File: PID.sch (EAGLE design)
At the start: 11 parts, among them IC1 UA741CPE4, IC2 UA741CPE4, IC3 UA741CPE4

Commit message: paf
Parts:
- added CONSIGNE, RETOUR, RETOUR1: (no value), pinhead:PINHD-1X1
- added IC4, IC5: UA741CPE4, SamacSys_Parts:UA741CPE4
- added R1, R3, R4, R6: 22k, rcl:R-EU_0204/7
- added R10, R7, R8, R9: 10k, rcl:R-EU_0204/7
- added R11: 2.5k, rcl:R-EU_0204/7
- added R5: (no value), rcl:R-EU_0204/7
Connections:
- new net CONSIGNE: CONSIGNE.1, R4.1
- new net N$13: IC5.IN+, R4.2, R6.2
- new net N$15: IC4.IN-, R10.1, R7.2, R8.2, R9.2
- new net N$17: C3.+, R5.2
- new net N$18: IC4.IN+, R11.2
- new net N$9: IC5.IN-, R1.1, R3.2
- new net OUTPUT: IC4.OUT, R10.2, RETOUR1.1
- new net RETOUR: R3.1, R5.1, RETOUR.1
- net GND: now also R11.1, R6.1
- net N$10: now also R9.1
- net N$2: now also R7.1
- net N$4: now also R8.1
- net N$7: now also IC5.OUT, R1.2, R2.1
- net V+: now also IC4.VCC+, IC5.VCC+
- net V-: now also IC4.VCC-, IC5.VCC-
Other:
- moved on the sheet: C1, C2, C3, C4, IC1, IC2, IC3, R2, VR1, VR2, VR3

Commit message: paf
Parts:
- removed C3, C4: (no value), rcl:CPOL-EUE2.5-6
- removed R5: (no value), rcl:R-EU_0204/7
- removed VR1, VR3: T7YA103MT20, PFE:T7YA103MT20
- added CD1, CD2: (no value), rcl:CPOL-EUE2.5-6
- added R13, R14: 22k, rcl:R-EU_0204/7
- added RD: T7YA103MT20, PFE:T7YA103MT20
- R1, R3: value 22k -> (none)
- R11: value 2.5k -> 5k
- R2: value (none) -> T7YA103MT20; device rcl:R-EU_0204/7 -> PFE:T7YA103MT20
- renumbered C1 to CI1, C2 to CI2, VR2 to RI
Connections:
- new net N$16: IC4.IN-, R10.1, R7.2, R8.2
- net N$10: now also RD.C; no longer VR3.C
- net N$12: now also CD2.+, RD.A, RD.B; no longer C4.+, VR3.A, VR3.B
- net N$14: now also CD1.-, CD2.-; no longer C3.-, C4.-
- net N$15: now also IC5.OUT, R13.2; no longer IC4.IN-, R10.1, R7.2, R8.2, R9.2
- net N$17: now also CD1.+, R3.2; no longer C3.+, R5.2
- net N$18: now also R9.2
- net N$2: now also R2.C; no longer VR1.C
- net N$3: now also R1.2, R2.A, R2.B; no longer R2.2, VR1.A, VR1.B
- net N$7: now also R1.1; no longer IC5.OUT, R1.2, R2.1
- net N$9: now also R13.1, R14.2; no longer R1.1, R3.2
- net RETOUR: now also R14.1; no longer R5.1
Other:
- moved on the sheet: IC1, IC3, R1, R3

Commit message: paf
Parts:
- removed RETOUR1: (no value), pinhead:PINHD-1X1
- added OUTPUT: (no value), pinhead:PINHD-1X1
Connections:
- removed net N$7 (its old number): R1.1, RI.A, RI.B
- net N$15: now also R1.1, RI.A, RI.B
- net OUTPUT: now also OUTPUT.1; no longer RETOUR1.1
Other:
- note added: "Comparateur"
- note added: "Sommeur"
- moved on the sheet: CONSIGNE, IC4, IC5, R10, R13, R14, R4, R6, R7, R8, R9, RETOUR

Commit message: paf
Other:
- note added: "Erreur"
- note added: "K = 1/(Ri*Ci)"
- note added: "K = R2/R1"
- note added: "K = Rd*Cd"
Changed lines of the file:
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@@
 <wire x1="261.62" y1="73.66" x2="190.5" y2="73.66" width="0.1524" layer="97"/>
 <text x="193.04" y="30.48" size="1.778" layer="97">Sommeur</text>
+<text x="63.5" y="71.12" size="1.778" layer="91">Erreur</text>
+<text x="147.32" y="48.26" size="1.778" layer="97">K = 1/(Ri*Ci)</text>
+<text x="149.86" y="99.06" size="1.778" layer="97">K = R2/R1</text>
+<text x="149.86" y="-5.08" size="1.778" layer="97">K = Rd*Cd</text>
 </plain>
 <instances>

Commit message: paf
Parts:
- added GND, V+, V-: (no value), pinhead:PINHD-1X1
- added S1, S2, S3: TL36PO, switch:TL36PO
- renumbered R1 to RP1, R2 to RP, R3 to RD1
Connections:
- new net N$12: R7.1, S1.P
- new net N$16: R8.1, S2.P
- new net N$19: R9.1, S3.P
- net GND: now also GND.1, S1.O, S2.O, S3.O
- net N$10: now also S3.S; no longer R9.1
- net N$2: now also S1.S; no longer R7.1
- net N$4: now also S2.S; no longer R8.1
- net V+: now also V+.1
- net V-: now also V-.1
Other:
- moved on the sheet: OUTPUT

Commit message: couocu
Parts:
- removed S1, S2, S3: TL36PO, switch:TL36PO
- added JP1, JP2, JP3: (no value), pinhead:PINHD-1X2
- added R1: 100k, rcl:R-EU_0204/7
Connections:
- net N$15 renamed ERREUR
- net GND: no longer S1.O, S2.O, S3.O
- net N$10: now also JP3.1; no longer S3.S
- net N$12: now also JP1.2; no longer S1.P
- net N$16: now also JP2.2; no longer S2.P
- net N$19: now also JP3.2; no longer S3.P
- net N$2: now also JP1.1; no longer S1.S
- net N$4: now also JP2.1, R1.2; no longer S2.S
- net N$5: now also R1.1
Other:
- note removed: "Erreur"
- moved on the sheet: CI1, CI2, CONSIGNE, GND, IC5, OUTPUT, R13, R14, R4, R6, RETOUR, V+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

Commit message: paf
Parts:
- added R2: 1k, rcl:R-EU_0204/7
- CD1, CD2: value (none) -> 10µ
- CI1, CI2: value (none) -> 470µ
- RD, RP: value T7YA103MT20 -> 10k
- RD1: value (none) -> 200
- RI: value T7YA103MT20 -> 100k
- RP1: value (none) -> 1k
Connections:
- new net N$15: R2.2, RI.A, RI.B
- net ERREUR: now also R2.1; no longer RI.A, RI.B
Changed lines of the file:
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@@
 <attribute name="SPICEPREFIX" value="X"/>
 </part>
-<part name="RP1" library="rcl" library_urn="urn:adsk.eagle:library:334" deviceset="R-EU_" device="0204/7" package3d_urn="urn:adsk.eagle:package:23498/2"/>
+<part name="RP1" library="rcl" library_urn="urn:adsk.eagle:library:334" deviceset="R-EU_" device="0204/7" package3d_urn="urn:adsk.eagle:package:23498/2" value="1k"/>
 <part name="SUPPLY1" library="supply2" library_urn="urn:adsk.eagle:library:372" deviceset="GND" device=""/>
 <part name="P-1" library="supply1" library_urn="urn:adsk.eagle:library:371" deviceset="V-" device=""/>
 <part name="P+2" library="supply1" library_urn="urn:adsk.eagle:library:371" deviceset="V+" device=""/>
-<part name="RP" library="PFE" deviceset="T7YA103MT20" device=""/>
+<part name="RP" library="PFE" deviceset="T7YA103MT20" device="" value="10k"/>
 <part name="IC2" library="SamacSys_Parts" deviceset="UA741CPE4" device="">
 <attribute name="SPICEMODEL" value="OPAMP"/>
@@
 <part name="P-2" library="supply1" library_urn="urn:adsk.eagle:library:371" deviceset="V-" device=""/>
 <part name="P+1" library="supply1" library_urn="urn:adsk.eagle:library:371" deviceset="V+" device=""/>
-<part name="RI" library="PFE" deviceset="T7YA103MT20" device=""/>
-<part name="CI1" library="rcl" library_urn="urn:adsk.eagle:library:334" deviceset="CPOL-EU" device="E2.5-6" package3d_urn="urn:adsk.eagle:package:23349/1"/>
-<part name="CI2" library="rcl" library_urn="urn:adsk.eagle:library:334" deviceset="CPOL-EU" device="E2.5-6" package3d_urn="urn:adsk.eagle:package:23349/1"/>
+<part name="RI" library="PFE" deviceset="T7YA103MT20" device="" value="100k"/>
+<part name="CI1" library="rcl" library_urn="urn:adsk.eagle:library:334" deviceset="CPOL-EU" device="E2.5-6" package3d_urn="urn:adsk.eagle:package:23349/1" value="470µ"/>
+<part name="CI2" library="rcl" library_urn="urn:adsk.eagle:library:334" deviceset="CPOL-EU" device="E2.5-6" package3d_urn="urn:adsk.eagle:package:23349/1" value="470µ"/>
 <part name="IC3" library="SamacSys_Parts" deviceset="UA741CPE4" device="">
 <attribute name="SPICEMODEL" value="OPAMP"/>
@@
 <part name="P-3" library="supply1" library_urn="urn:adsk.eagle:library:371" deviceset="V-" device=""/>
 <part name="P+3" library="supply1" library_urn="urn:adsk.eagle:library:371" deviceset="V+" device=""/>
-<part name="RD" library="PFE" deviceset="T7YA103MT20" device=""/>
-<part name="CD1" library="rcl" library_urn="urn:adsk.eagle:library:334" deviceset="CPOL-EU" device="E2.5-6" package3d_urn="urn:adsk.eagle:package:23349/1"/>
-<part name="CD2" library="rcl" library_urn="urn:adsk.eagle:library:334" deviceset="CPOL-EU" device="E2.5-6" package3d_urn="urn:adsk.eagle:package:23349/1"/>
+<part name="RD" library="PFE" deviceset="T7YA103MT20" device="" value="10k"/>
+<part name="CD1" library="rcl" library_urn="urn:adsk.eagle:library:334" deviceset="CPOL-EU" device="E2.5-6" package3d_urn="urn:adsk.eagle:package:23349/1" value="10µ"/>
+<part name="CD2" library="rcl" library_urn="urn:adsk.eagle:library:334" deviceset="CPOL-EU" device="E2.5-6" package3d_urn="urn:adsk.eagle:package:23349/1" value="10µ"/>
 <part name="IC5" library="SamacSys_Parts" deviceset="UA741CPE4" device="">
 <attribute name="SPICEMODEL" value="OPAMP"/>
@@
 <part name="CONSIGNE" library="pinhead" library_urn="urn:adsk.eagle:library:325" deviceset="PINHD-1X1" device="" package3d_urn="urn:adsk.eagle:package:22485/2"/>
 <part name="RETOUR" library="pinhead" library_urn="urn:adsk.eagle:library:325" deviceset="PINHD-1X1" device="" package3d_urn="urn:adsk.eagle:package:22485/2"/>
-<part name="RD1" library="rcl" library_urn="urn:adsk.eagle:library:334" deviceset="R-EU_" device="0204/7" package3d_urn="urn:adsk.eagle:package:23498/2"/>
+<part name="RD1" library="rcl" library_urn="urn:adsk.eagle:library:334" deviceset="R-EU_" device="0204/7" package3d_urn="urn:adsk.eagle:package:23498/2" value="200"/>
 <part name="R6" library="rcl" library_urn="urn:adsk.eagle:library:334" deviceset="R-EU_" device="0204/7" package3d_urn="urn:adsk.eagle:package:23498/2" value="22k"/>
 <part name="SUPPLY4" library="supply2" library_urn="urn:adsk.eagle:library:372" deviceset="GND" device=""/>
@@
 <part name="JP3" library="pinhead" library_urn="urn:adsk.eagle:library:325" deviceset="PINHD-1X2" device="" package3d_urn="urn:adsk.eagle:package:22435/2"/>
 <part name="R1" library="rcl" library_urn="urn:adsk.eagle:library:334" deviceset="R-EU_" device="0204/7" package3d_urn="urn:adsk.eagle:package:23498/2" value="100k"/>
+<part name="R2" library="rcl" library_urn="urn:adsk.eagle:library:334" deviceset="R-EU_" device="0204/7" package3d_urn="urn:adsk.eagle:package:23498/2" value="1k"/>
 </parts>
 <sheets>
@@
 <attribute name="VALUE" x="128.27" y="72.898" size="1.778" layer="96"/>
 </instance>
+<instance part="R2" gate="G$1" x="76.2" y="63.5" smashed="yes">
+<attribute name="NAME" x="72.39" y="64.9986" size="1.778" layer="95"/>
+<attribute name="VALUE" x="72.39" y="60.198" size="1.778" layer="96"/>
+</instance>
 </instances>
 <busses>
@@
 <net name="ERREUR" class="0">
 <segment>
-<pinref part="RI" gate="G$1" pin="A"/>
-<pinref part="RI" gate="G$1" pin="B"/>
-<wire x1="83.82" y1="60.96" x2="83.82" y2="63.5" width="0.1524" layer="91"/>
-<wire x1="83.82" y1="63.5" x2="68.58" y2="63.5" width="0.1524" layer="91"/>
-<junction x="83.82" y="63.5"/>
 <pinref part="RP1" gate="G$1" pin="1"/>
 <wire x1="93.98" y1="111.76" x2="68.58" y2="111.76" width="0.1524" layer="91"/>
@@
 <label x="71.12" y="99.06" size="1.778" layer="95" rot="R90"/>
 <pinref part="R13" gate="G$1" pin="2"/>
+<wire x1="68.58" y1="63.5" x2="68.58" y2="48.26" width="0.1524" layer="91"/>
 <wire x1="55.88" y1="66.04" x2="33.02" y2="66.04" width="0.1524" layer="91"/>
 <wire x1="55.88" y1="48.26" x2="55.88" y2="66.04" width="0.1524" layer="91"/>
@@
 <wire x1="55.88" y1="48.26" x2="68.58" y2="48.26" width="0.1524" layer="91"/>
 <junction x="55.88" y="48.26"/>
-<wire x1="68.58" y1="48.26" x2="68.58" y2="63.5" width="0.1524" layer="91"/>
+<pinref part="R2" gate="G$1" pin="1"/>
+<wire x1="71.12" y1="63.5" x2="68.58" y2="63.5" width="0.1524" layer="91"/>
 <junction x="68.58" y="63.5"/>
 </segment>
@@
 </segment>
 </net>
+<net name="N$15" class="0">
+<segment>
+<pinref part="RI" gate="G$1" pin="A"/>
+<pinref part="RI" gate="G$1" pin="B"/>
+<wire x1="83.82" y1="60.96" x2="83.82" y2="63.5" width="0.1524" layer="91"/>
+<pinref part="R2" gate="G$1" pin="2"/>
+<wire x1="81.28" y1="63.5" x2="83.82" y2="63.5" width="0.1524" layer="91"/>
+<junction x="83.82" y="63.5"/>
+</segment>
+</net>

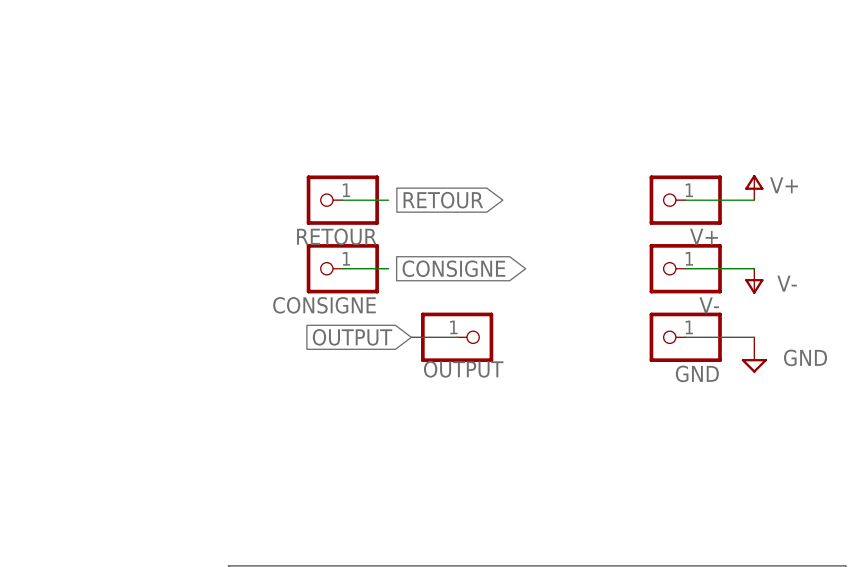
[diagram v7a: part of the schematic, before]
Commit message: Le routage de lavage, tous les signaux sur le bottom, le plan de masse sur le bottom, plan de V- sur le top et routage du V+ sur le top
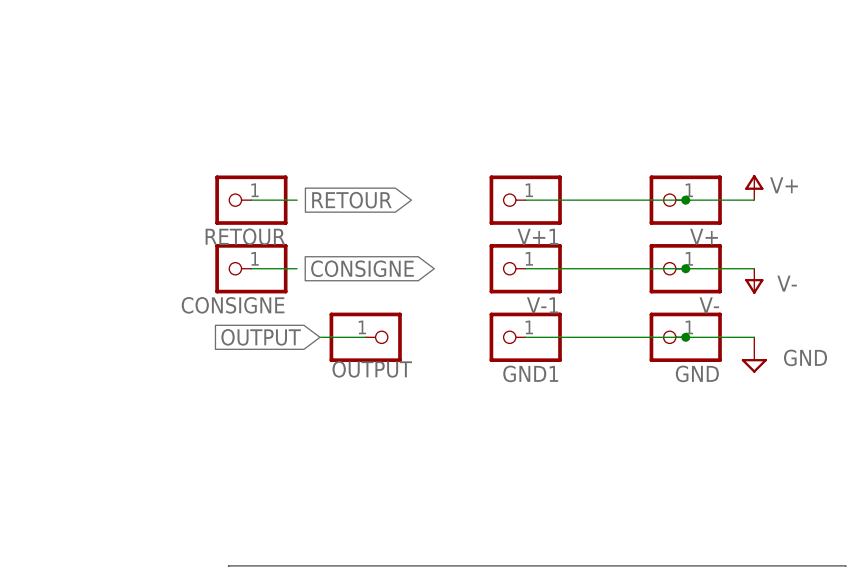
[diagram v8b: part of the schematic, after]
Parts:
- added GND1, V+1, V-1: (no value), pinhead:PINHD-1X1
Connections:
- net GND: now also GND1.1
- net V+: now also V+1.1
- net V-: now also V-1.1
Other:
- moved on the sheet: CONSIGNE, OUTPUT, RETOUR
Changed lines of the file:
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@@
 <?xml version="1.0" encoding="utf-8"?>
 <!DOCTYPE eagle SYSTEM "eagle.dtd">
-<eagle version="9.5.1">
+<eagle version="9.5.2">
 <drawing>
 <settings>
@@
 <part name="R1" library="rcl" library_urn="urn:adsk.eagle:library:334" deviceset="R-EU_" device="0204/7" package3d_urn="urn:adsk.eagle:package:23498/2" value="100k"/>
 <part name="R2" library="rcl" library_urn="urn:adsk.eagle:library:334" deviceset="R-EU_" device="0204/7" package3d_urn="urn:adsk.eagle:package:23498/2" value="1k"/>
+<part name="V-1" library="pinhead" library_urn="urn:adsk.eagle:library:325" deviceset="PINHD-1X1" device="" package3d_urn="urn:adsk.eagle:package:22485/2"/>
+<part name="V+1" library="pinhead" library_urn="urn:adsk.eagle:library:325" deviceset="PINHD-1X1" device="" package3d_urn="urn:adsk.eagle:package:22485/2"/>
+<part name="GND1" library="pinhead" library_urn="urn:adsk.eagle:library:325" deviceset="PINHD-1X1" device="" package3d_urn="urn:adsk.eagle:package:22485/2"/>
 </parts>
 <sheets>
@@
 <attribute name="VALUE" x="-6.35" y="42.418" size="1.778" layer="96"/>
 </instance>
-<instance part="CONSIGNE" gate="G$1" x="0" y="104.14" smashed="yes" rot="R180">
-<attribute name="NAME" x="6.35" y="100.965" size="1.778" layer="95" rot="R180"/>
-<attribute name="VALUE" x="6.35" y="109.22" size="1.778" layer="96" rot="R180"/>
-</instance>
-<instance part="RETOUR" gate="G$1" x="0" y="111.76" smashed="yes" rot="R180">
-<attribute name="NAME" x="6.35" y="108.585" size="1.778" layer="95" rot="R180"/>
-<attribute name="VALUE" x="6.35" y="116.84" size="1.778" layer="96" rot="R180"/>
+<instance part="CONSIGNE" gate="G$1" x="-10.16" y="104.14" smashed="yes" rot="R180">
+<attribute name="NAME" x="-3.81" y="100.965" size="1.778" layer="95" rot="R180"/>
+<attribute name="VALUE" x="-3.81" y="109.22" size="1.778" layer="96" rot="R180"/>
+</instance>
+<instance part="RETOUR" gate="G$1" x="-10.16" y="111.76" smashed="yes" rot="R180">
+<attribute name="NAME" x="-3.81" y="108.585" size="1.778" layer="95" rot="R180"/>
+<attribute name="VALUE" x="-3.81" y="116.84" size="1.778" layer="96" rot="R180"/>
 </instance>
 <instance part="RD1" gate="G$1" x="83.82" y="12.7" smashed="yes">
@@
 <attribute name="VALUE" x="198.755" y="37.465" size="1.778" layer="96"/>
 </instance>
-<instance part="OUTPUT" gate="G$1" x="17.78" y="96.52" smashed="yes">
-<attribute name="NAME" x="11.43" y="92.075" size="1.778" layer="95"/>
-<attribute name="VALUE" x="11.43" y="91.44" size="1.778" layer="96"/>
+<instance part="OUTPUT" gate="G$1" x="7.62" y="96.52" smashed="yes">
+<attribute name="NAME" x="1.27" y="92.075" size="1.778" layer="95"/>
+<attribute name="VALUE" x="1.27" y="91.44" size="1.778" layer="96"/>
 </instance>
 <instance part="V-" gate="G$1" x="38.1" y="104.14" smashed="yes" rot="R180">
@@
 <attribute name="NAME" x="72.39" y="64.9986" size="1.778" layer="95"/>
 <attribute name="VALUE" x="72.39" y="60.198" size="1.778" layer="96"/>
+</instance>
+<instance part="V-1" gate="G$1" x="20.32" y="104.14" smashed="yes" rot="R180">
+<attribute name="NAME" x="26.67" y="100.965" size="1.778" layer="95" rot="R180"/>
+<attribute name="VALUE" x="26.67" y="109.22" size="1.778" layer="96" rot="R180"/>
+</instance>
+<instance part="V+1" gate="G$1" x="20.32" y="111.76" smashed="yes" rot="R180">
+<attribute name="NAME" x="26.67" y="108.585" size="1.778" layer="95" rot="R180"/>
+<attribute name="VALUE" x="26.67" y="116.84" size="1.778" layer="96" rot="R180"/>
+</instance>
+<instance part="GND1" gate="G$1" x="20.32" y="96.52" smashed="yes" rot="R180">
+<attribute name="NAME" x="26.67" y="93.345" size="1.778" layer="95" rot="R180"/>
+<attribute name="VALUE" x="26.67" y="101.6" size="1.778" layer="96" rot="R180"/>
 </instance>
 </instances>
@@
 <pinref part="SUPPLY6" gate="GND" pin="GND"/>
 <wire x1="40.64" y1="96.52" x2="48.26" y2="96.52" width="0.1524" layer="91"/>
+<pinref part="GND1" gate="G$1" pin="1"/>
+<wire x1="22.86" y1="96.52" x2="40.64" y2="96.52" width="0.1524" layer="91"/>
+<junction x="40.64" y="96.52"/>
 </segment>
 </net>
@@
 <pinref part="P-6" gate="1" pin="V-"/>
 <wire x1="40.64" y1="104.14" x2="48.26" y2="104.14" width="0.1524" layer="91"/>
+<pinref part="V-1" gate="G$1" pin="1"/>
+<wire x1="22.86" y1="104.14" x2="40.64" y2="104.14" width="0.1524" layer="91"/>
+<junction x="40.64" y="104.14"/>
 </segment>
 </net>
@@
 <pinref part="P+6" gate="1" pin="V+"/>
 <wire x1="40.64" y1="111.76" x2="48.26" y2="111.76" width="0.1524" layer="91"/>
+<pinref part="V+1" gate="G$1" pin="1"/>
+<wire x1="22.86" y1="111.76" x2="40.64" y2="111.76" width="0.1524" layer="91"/>
+<junction x="40.64" y="111.76"/>
 </segment>
 </net>
@@
 <segment>
 <pinref part="RETOUR" gate="G$1" pin="1"/>
-<wire x1="2.54" y1="111.76" x2="7.62" y2="111.76" width="0.1524" layer="91"/>
-<label x="20.32" y="111.76" size="1.778" layer="95" rot="R180" xref="yes"/>
+<wire x1="-7.62" y1="111.76" x2="-2.54" y2="111.76" width="0.1524" layer="91"/>
+<label x="10.16" y="111.76" size="1.778" layer="95" rot="R180" xref="yes"/>
 </segment>
 <segment>
@@
 <segment>
 <pinref part="CONSIGNE" gate="G$1" pin="1"/>
-<wire x1="2.54" y1="104.14" x2="7.62" y2="104.14" width="0.1524" layer="91"/>
-<label x="22.86" y="104.14" size="1.778" layer="95" rot="R180" xref="yes"/>
+<wire x1="-7.62" y1="104.14" x2="-2.54" y2="104.14" width="0.1524" layer="91"/>
+<label x="12.7" y="104.14" size="1.778" layer="95" rot="R180" xref="yes"/>
 </segment>
 <segment>
@@
 <segment>
 <pinref part="OUTPUT" gate="G$1" pin="1"/>
-<wire x1="15.24" y1="96.52" x2="10.16" y2="96.52" width="0.1524" layer="91"/>
-<label x="10.16" y="96.52" size="1.778" layer="95" rot="R180" xref="yes"/>
-</segment>
-</net>
+<wire x1="5.08" y1="96.52" x2="0" y2="96.52" width="0.1524" layer="91"/>
+<label x="0" y="96.52" size="1.778" layer="95" rot="R180" xref="yes"/>
+</segment>
+</net>
